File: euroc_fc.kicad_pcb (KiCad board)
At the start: 4 copper layers, 50 x 100 mm, 123 parts, among them J1 Micro-Fit, J10 USB_C_Receptacle_USB2.0, J2 Micro-Fit, J3 Micro-Fit, J4 SMA, J5 JST-GH, J6 JST-GH, J7 JST-GH, J8 JST-GH, J9 Micro_SD_Card_Det, Q1 DMG2302U, Q2 AOSP21321, Q3 DMG2302U, Q4 AOSP21321, Q5 DMG2302U, Q6 DMG2302U, Q7 DMG2302U, SW1 EVQ-PUC02K, SW2 EVQ-PUC02K, U1 STM32F401RCT6, U10 Ai-Thinker-Ra-01, U11 W25Q256JVF, U2 L7805, U3 L7805, U4 AZ1117I-3.3, U5 LSM6DSR, U6 ADXL375, U7 MS5611-01BA, U8 BMM150, U9 SAM-M8Q, Y1 25M

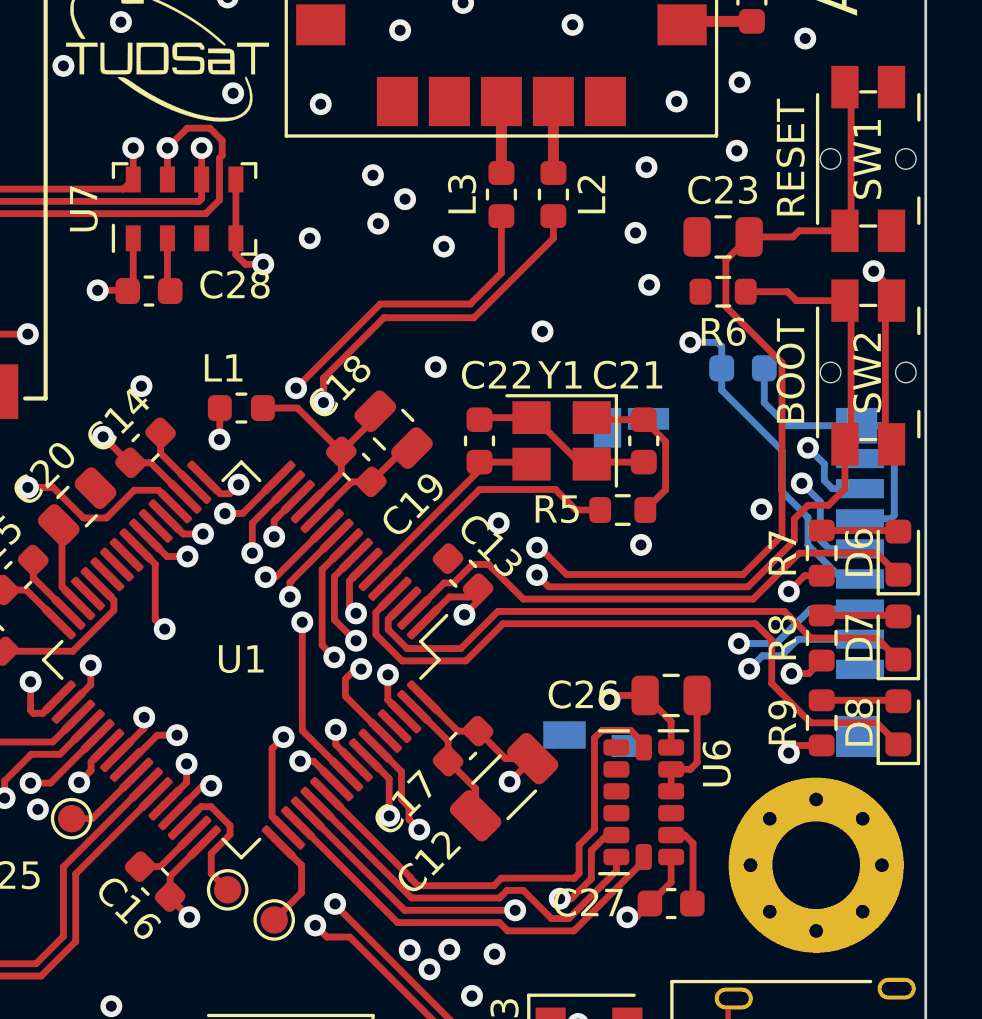
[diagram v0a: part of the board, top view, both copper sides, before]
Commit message: Update part selection, complete BOM
- Voltage divider reduced to 1k / (1k + 1k8)
- Diode changed to onsemi SS26FL (higher current capacity)
- N-Ch. MOSFET changed to DMN2056U (official successor)
- uSD holder changed to Hirose DM3AT (push-push)
- Vendor and Datasheet fields filled out for (almost) all components
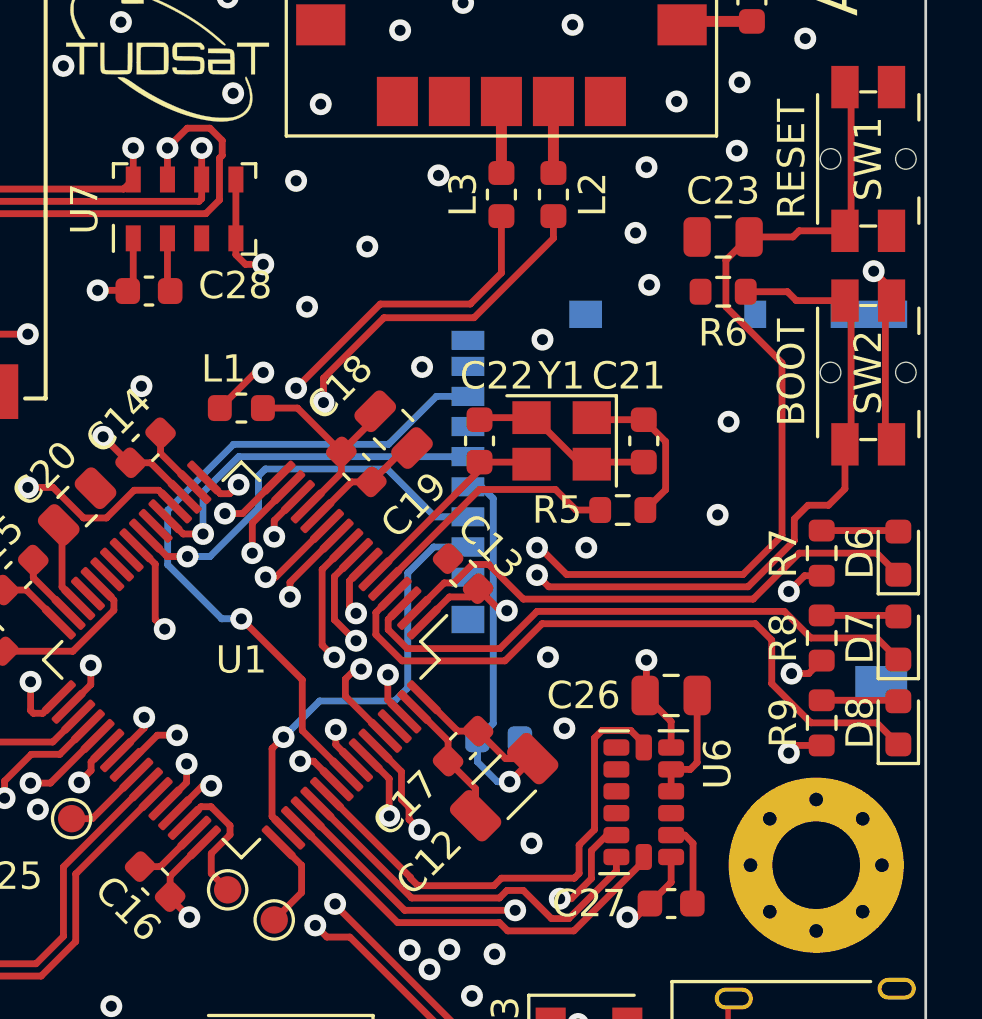
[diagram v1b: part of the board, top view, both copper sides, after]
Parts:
- D1, D2, D3: value DSS16UTR -> SS26FL
- J9: footprint Connector_Card:microSD_HC_Hirose_DM3D-SF -> Connector_Card:microSD_HC_Hirose_DM3AT-SF-PEJM5
- Q1, Q3, Q5, Q6, Q7: value DMG2302U -> DMN2056U
- R1: value 10m -> 10m, 1%, 2W
- R10, R12, R14: value 3k3 -> 1k8
- moved C39 16.2 mm to (109.4, 95.4)
- moved J9 3.22 mm to (116.0, 86.7)
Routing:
- net SPI1_MOSI: track 117.7 -> 92.8 mm, vias 7 -> 5
- net SPI1_SCL: track 106.3 -> 82.4 mm, vias 7 -> 5
- net SPI1_CS_SD: track 27.2 -> 16.0 mm, vias 2 -> 1
- net GND: track 79.8 -> 69.2 mm, vias 105 -> 110
- net SPI1_MISO: track 114.8 -> 106.1 mm, vias 7 -> 5
- net +3V3: track 98.2 -> 99.6 mm, vias 28 -> 27

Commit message: Tweak LoRa trans line impedance, power planes
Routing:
- net GND: vias 110 -> 126
- added copper zone on In1.Cu, net GND
- added copper zone on In2.Cu, net GND
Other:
- board text added: "Sting"
- board text removed: "AthenaFC"

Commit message: Tweak via grouping for power planes
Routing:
- net RADIO_IRQ: track 47.4 -> 49.1 mm
- net SPI1_MISO: track 106.1 -> 105.0 mm
- net +3V3: track 99.6 -> 100.6 mm, vias 27 -> 29
- net RADIO_RESET: track 49.6 -> 48.7 mm
- net GND: vias 126 -> 122
